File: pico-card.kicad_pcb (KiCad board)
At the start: 2 copper layers, 84 parts, among them J1 Conn_02x05_Odd_Even, J2 USB_C_Receptacle_USB2.0, J3 Conn_02x05_Odd_Even, J4 Conn_02x05_Odd_Even, U1 AP2112K-3.3, U2 ATECC608A-SSHDA, U3 W25Q128JVS, U4 RP2040, Y1 Crystal_GND24

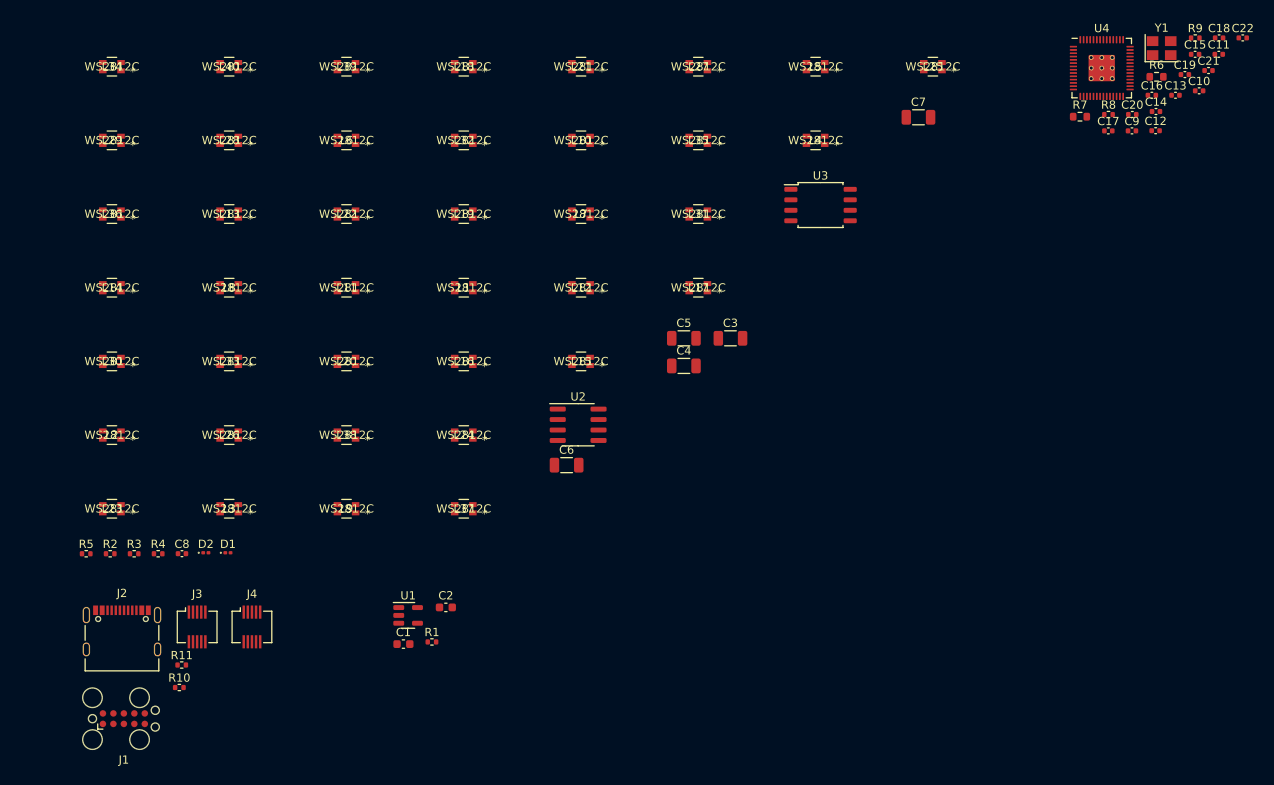
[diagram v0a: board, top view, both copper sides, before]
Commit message: Basic routing MCU, crystal, flash, crypto
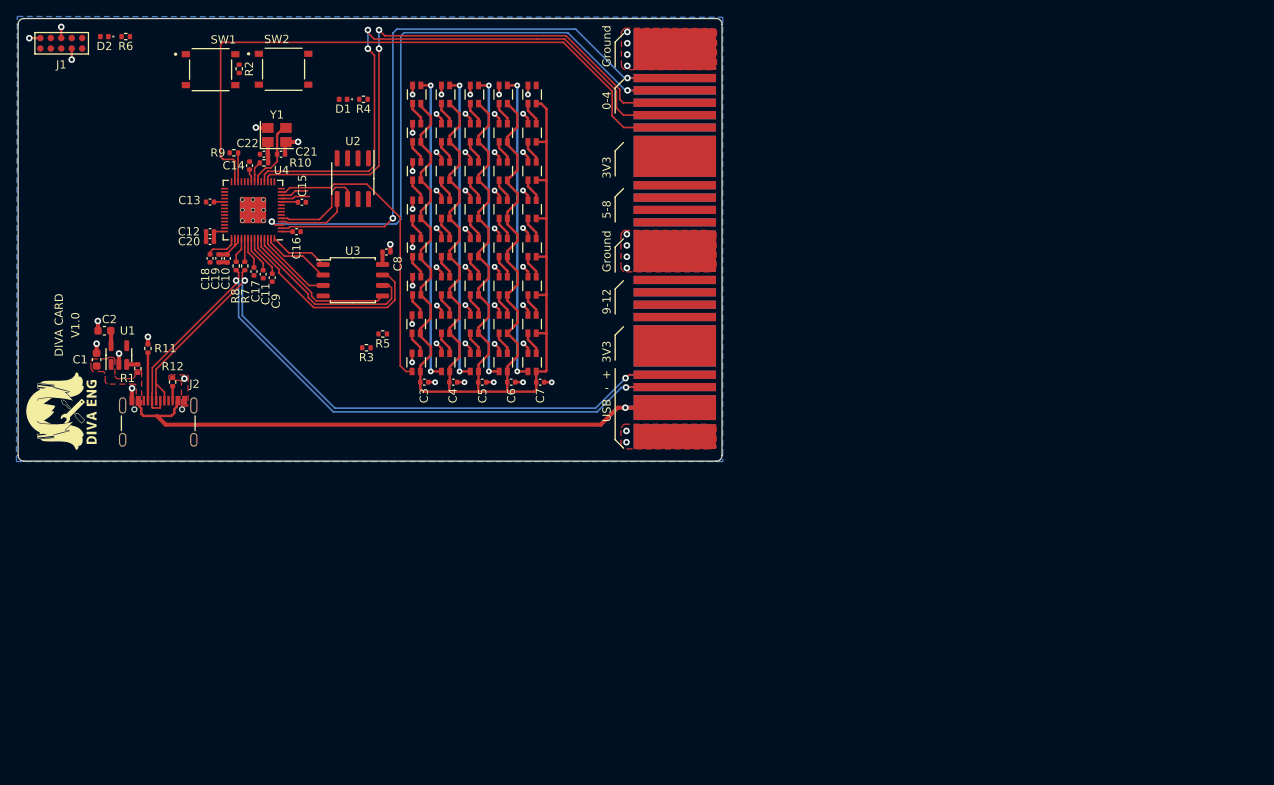
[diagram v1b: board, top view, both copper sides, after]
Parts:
- removed J4: Conn_02x05_Odd_Even, Connector_Hirose:Hirose_DF12_DF12C3.0-10DS-0.5V_2x05_P0.50mm_Vertical
- added G***: LOGO, LOGO, F.Cu at (69.1, 108.2)
- added R2: 5k, Resistor_SMD:R_0402_1005Metric, F.Cu at (90.4, 66.8)
- added SW1: SW_Push, pico-card:SW_TS-1187A-B-A-B, F.Cu at (87.0, 66.9)
- added SW2: SW_Push, pico-card:SW_TS-1187A-B-A-B, F.Cu at (95.8, 66.8)
- C3, C4, C5, C6, C7: value 100u -> 100n; footprint Capacitor_SMD:C_1206_3216Metric -> Capacitor_SMD:C_0402_1005Metric
- D1, D2: footprint LED_SMD:LED_0201_0603Metric -> LED_SMD:LED_0402_1005Metric
- J1: footprint Connector:Tag-Connect_TC2050-IDC-FP_2x05_P1.27mm_Vertical -> Connector:Tag-Connect_TC2050-IDC-NL_2x05_P1.27mm_Vertical
- J3: value Conn_02x05_Odd_Even -> Conn_02x21_Odd_Even; footprint Connector_Hirose:Hirose_DF12_DF12C3.0-10DS-0.5V_2x05_P0.50mm_Vertical -> pico-card:PICO_CARD_EDGE_21
- R7: renamed from R6; footprint Resistor_SMD:R_0603_1608Metric -> Resistor_SMD:R_0402_1005Metric
- R8: renamed from R7; footprint Resistor_SMD:R_0603_1608Metric -> Resistor_SMD:R_0402_1005Metric
- moved C18 125.3 mm to (86.9, 89.8), turned to -90 degrees
- moved C10 119.7 mm to (89.0, 89.8), turned to -90 degrees
- moved C22 119.6 mm to (93.4, 77.1)
- moved C19 119.3 mm to (88.0, 89.8), turned to -90 degrees
- moved C11 119.0 mm to (93.3, 91.7), turned to -90 degrees
- moved C13 117.9 mm to (86.9, 82.9), turned to 180 degrees
- moved C12 115.4 mm to (86.9, 86.5), turned to 180 degrees
- moved R10 114.0 mm to (93.4, 78.2), turned to 180 degrees
- moved C21 113.0 mm to (95.5, 77.1), turned to 180 degrees
- moved R7 113.0 mm to (91.1, 90.7), turned to -90 degrees
- moved C20 113.0 mm to (86.9, 87.7), turned to 180 degrees
- moved C14 110.2 mm to (91.7, 78.5), turned to 90 degrees
- moved C15 109.9 mm to (98.0, 82.9)
- moved Y1 107.9 mm to (95.0, 74.8)
- moved R9 106.2 mm to (89.8, 76.9)
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- renumbered R9 to R10, R10 to R11, R11 to R12, R2 to R3, R3 to R4, R4 to R5, R5 to R6, R8 to R9
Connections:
- net /microcontroller/GPIO_02 renamed /I2C0_SDA
- net /microcontroller/GPIO_03 renamed /I2C0_SCL
- net /microcontroller/GPIO_09 renamed /USER_LED
- net /microcontroller/GPIO_10 renamed /LED_DI
- C3 pad 1: +5V -> VBUS
- C4 pad 1: +5V -> VBUS
- C5 pad 1: +5V -> VBUS
- C6 pad 1: +5V -> VBUS
- C7 pad 1: +5V -> VBUS
- J3 pad 2: +3V3 -> GND
- J3 pad 3: GND -> /connectors/USER_IO_0
- J3 pad 5: GND -> /connectors/USER_IO_1
- J3 pad 7: GND -> /connectors/USER_IO_2
- J3 pad 9: GND -> /connectors/USER_IO_3
- L1 pad 4: +5V -> VBUS
- L10 pad 4: +5V -> VBUS
- L11 pad 4: +5V -> VBUS
- L12 pad 4: +5V -> VBUS
- L13 pad 4: +5V -> VBUS
- L14 pad 4: +5V -> VBUS
- L15 pad 4: +5V -> VBUS
- L16 pad 4: +5V -> VBUS
- L17 pad 4: +5V -> VBUS
- L18 pad 4: +5V -> VBUS
- L19 pad 4: +5V -> VBUS
- L2 pad 4: +5V -> VBUS
- L20 pad 4: +5V -> VBUS
- L21 pad 4: +5V -> VBUS
- L22 pad 4: +5V -> VBUS
- L23 pad 4: +5V -> VBUS
- L24 pad 4: +5V -> VBUS
- L25 pad 4: +5V -> VBUS
- L26 pad 4: +5V -> VBUS
- L27 pad 4: +5V -> VBUS
- L28 pad 4: +5V -> VBUS
- L29 pad 4: +5V -> VBUS
- L3 pad 4: +5V -> VBUS
- L30 pad 4: +5V -> VBUS
- L31 pad 4: +5V -> VBUS
- L32 pad 4: +5V -> VBUS
- L33 pad 4: +5V -> VBUS
- L34 pad 4: +5V -> VBUS
- L35 pad 4: +5V -> VBUS
- L36 pad 4: +5V -> VBUS
- L37 pad 4: +5V -> VBUS
- L38 pad 4: +5V -> VBUS
- L39 pad 4: +5V -> VBUS
- L4 pad 4: +5V -> VBUS
- L40 pad 4: +5V -> VBUS
- L5 pad 4: +5V -> VBUS
- L6 pad 4: +5V -> VBUS
- L7 pad 4: +5V -> VBUS
- L8 pad 4: +5V -> VBUS
- L9 pad 4: +5V -> VBUS
- R7 pad 1: Net-(R6-Pad1) -> /connectors/USB_D+
- R8 pad 1: Net-(R7-Pad1) -> /connectors/USB_D-
- U4 pad 15: /connectors/USER_IO_0 -> /microcontroller/GPIO_12
- U4 pad 16: /connectors/USER_IO_1 -> /microcontroller/GPIO_13
- U4 pad 2: /microcontroller/GPIO_00 -> /connectors/USER_IO_0
- U4 pad 3: /microcontroller/GPIO_01 -> /connectors/USER_IO_1
- U4 pad 31: /microcontroller/GPIO_20 -> /connectors/USER_IO_8
- U4 pad 32: /microcontroller/GPIO_21 -> /connectors/USER_IO_9
- U4 pad 34: /microcontroller/GPIO_22 -> /connectors/USER_IO_10
- U4 pad 35: /microcontroller/GPIO_23 -> /connectors/USER_IO_11
- U4 pad 36: /microcontroller/GPIO_24 -> /connectors/USER_IO_12
- U4 pad 46: Net-(R7-Pad1) -> /connectors/USB_D-
- U4 pad 47: Net-(R6-Pad1) -> /connectors/USB_D+
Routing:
- net VBUS: track 0.00 -> 304.8 mm, vias 0 -> 1
- net /connectors/USB_D-: track 0.00 -> 95.5 mm, vias 0 -> 2
- net /connectors/USB_D+: track 0.00 -> 95.2 mm, vias 0 -> 2
- net /connectors/USER_IO_1: track 0.00 -> 81.6 mm, vias 0 -> 2
- net /connectors/USER_IO_4: track 0.00 -> 79.4 mm
- net /connectors/USER_IO_0: track 0.00 -> 79.1 mm, vias 0 -> 2
- net GND: track 0.00 -> 75.7 mm, vias 0 -> 67
- net /connectors/USER_IO_3: track 0.00 -> 74.4 mm, vias 0 -> 2
- net /connectors/USER_IO_2: track 0.00 -> 71.4 mm, vias 0 -> 2
- net Net-(L8-Pad1): track 0.00 -> 37.2 mm, vias 0 -> 2
- net Net-(L32-Pad1): track 0.00 -> 37.2 mm, vias 0 -> 2
- net Net-(L24-Pad1): track 0.00 -> 37.2 mm, vias 0 -> 2
- net Net-(L16-Pad1): track 0.00 -> 37.2 mm, vias 0 -> 2
- net /LED_DI: track 0.00 -> 36.2 mm
- net /microcontroller/QSPI_SIO3: track 0.00 -> 25.4 mm
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- added copper zone on B.Cu, net GND
- added copper zone on F.Cu, net GND
- added copper zone on F.Cu, net VBUS
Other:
- board outline added: 85.4 x 53.7 mm
- board text added: "+ -"
- board text added: "0-4"
- board text added: "3V3"
- board text added: "5-8"
- board text added: "9-12"
- board text added: "DIVA CARD"
- board text added: "Ground"
- board text added: "USB"
- board text added: "V1.0"
